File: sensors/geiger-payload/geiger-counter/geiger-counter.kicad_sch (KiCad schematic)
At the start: 38 parts, among them J1 3531, J2 3531, J4 Conn_02x03_Odd_Even, J5 Conn_01x06, J6 Conn_01x03, Q1 MMBTA44, Q2 MMBT3904, Q3 MMBT3904, SW1 SW_Push, SW2 SW_SPDT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

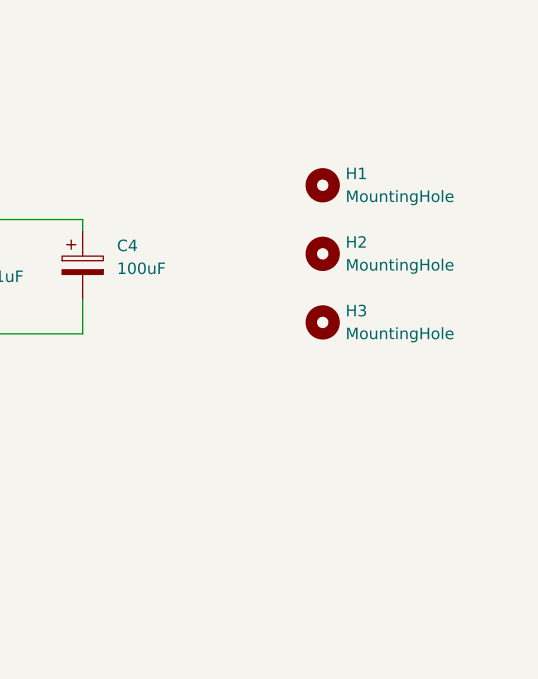
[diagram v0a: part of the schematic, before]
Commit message: Add pcb corrections
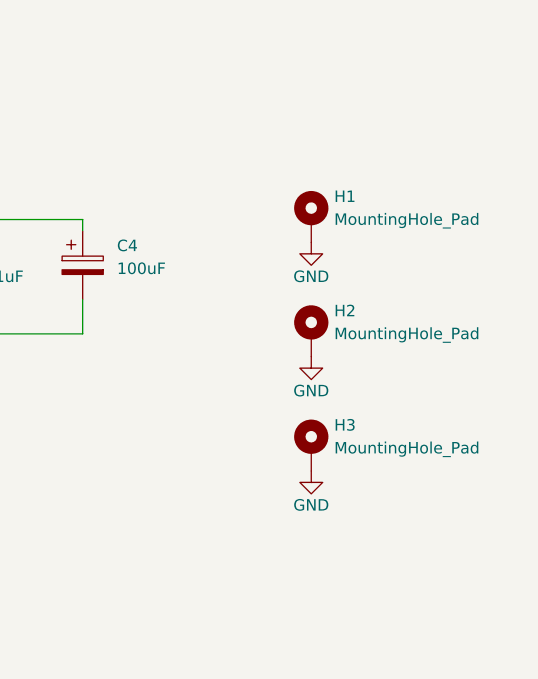
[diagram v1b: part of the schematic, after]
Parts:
- removed H1, H2, H3: MountingHole, MountingHole:MountingHole_2.2mm_M2_DIN965_Pad_TopOnly, symbol Mechanical:MountingHole
- added H1, H2, H3: MountingHole_Pad, MountingHole:MountingHole_2.2mm_M2_Pad, symbol Mechanical:MountingHole_Pad
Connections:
- net GND: now also H1.1, H2.1, H3.1
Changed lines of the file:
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@@
+    )
+  )
+  (symbol (lib_id "Mechanical:MountingHole_Pad") (at 250.19 133.35 0) (unit 1)
+    (in_bom yes) (on_board yes) (dnp no) (fields_autoplaced)
+    (property "Reference" "H3" (at 252.73 130.81 0)
+      (effects (font (size 1.27 1.27)) (justify left))
+    )
+    (property "Value" "MountingHole_Pad" (at 252.73 133.35 0)
+      (effects (font (size 1.27 1.27)) (justify left))
+    )
+    (property "Footprint" "MountingHole:MountingHole_2.2mm_M2_Pad" (at 250.19 133.35 0)
+      (effects (font (size 1.27 1.27)) hide)
+    )
+    (property "Datasheet" "~" (at 250.19 133.35 0)
+      (effects (font (size 1.27 1.27)) hide)
+    )
+    (pin "1")
+    (instances
+      (project "geiger-counter"
+        (path "/7804f9af-0587-435d-9482-64f925891946"
+          (reference "H3") (unit 1)
+        )
+      )
     )
   )
@@
         (path "/7804f9af-0587-435d-9482-64f925891946"
           (reference "#PWR08") (unit 1)
+        )
+      )
+    )
+  )
+  (symbol (lib_id "Mechanical:MountingHole_Pad") (at 250.19 107.95 0) (unit 1)
+    (in_bom yes) (on_board yes) (dnp no) (fields_autoplaced)
+    (property "Reference" "H1" (at 252.73 105.41 0)
+      (effects (font (size 1.27 1.27)) (justify left))
+    )
+    (property "Value" "MountingHole_Pad" (at 252.73 107.95 0)
+      (effects (font (size 1.27 1.27)) (justify left))
+    )
+    (property "Footprint" "MountingHole:MountingHole_2.2mm_M2_Pad" (at 250.19 107.95 0)
+      (effects (font (size 1.27 1.27)) hide)
+    )
+    (property "Datasheet" "~" (at 250.19 107.95 0)
+      (effects (font (size 1.27 1.27)) hide)
+    )
+    (pin "1")
+    (instances
+      (project "geiger-counter"
+        (path "/7804f9af-0587-435d-9482-64f925891946"
+          (reference "H1") (unit 1)
         )
       )
@@
     )
   )
+  (symbol (lib_id "power:GND") (at 250.19 123.19 0) (unit 1)
+    (in_bom yes) (on_board yes) (dnp no)
+    (property "Reference" "#PWR032" (at 250.19 129.54 0)
+      (effects (font (size 1.27 1.27)) hide)
+    )
+    (property "Value" "GND" (at 250.19 127 0)
+      (effects (font (size 1.27 1.27)))
+    )
+    (property "Footprint" "" (at 250.19 123.19 0)
+      (effects (font (size 1.27 1.27)) hide)
+    )
+    (property "Datasheet" "" (at 250.19 123.19 0)
+      (effects (font (size 1.27 1.27)) hide)
+    )
+    (pin "1")
+    (instances
+      (project "geiger-counter"
+        (path "/7804f9af-0587-435d-9482-64f925891946"
+          (reference "#PWR032") (unit 1)
+        )
+      )
+    )
+  )
   (symbol (lib_id "Transistor_BJT:MMBT3904") (at 104.14 55.88 0) (mirror y) (unit 1)
     (in_bom yes) (on_board yes) (dnp no)
@@
     )
   )
-  (symbol (lib_id "Mechanical:MountingHole") (at 251.46 104.14 0) (unit 1)
-    (in_bom yes) (on_board yes) (dnp no) (fields_autoplaced)
-    (property "Reference" "H1" (at 254 102.87 0)
-      (effects (font (size 1.27 1.27)) (justify left))
-    )
-    (property "Value" "MountingHole" (at 254 105.41 0)
-      (effects (font (size 1.27 1.27)) (justify left))
-    )
-    (property "Footprint" "MountingHole:MountingHole_2.2mm_M2_DIN965_Pad_TopOnly" (at 251.46 104.14 0)
-      (effects (font (size 1.27 1.27)) hide)
-    )
-    (property "Datasheet" "~" (at 251.46 104.14 0)
-      (effects (font (size 1.27 1.27)) hide)
-    )
-    (instances
-      (project "geiger-counter"
-        (path "/7804f9af-0587-435d-9482-64f925891946"
-          (reference "H1") (unit 1)
-        )
-      )
-    )
-  )
   (symbol (lib_id "Device:C") (at 80.01 78.74 0) (unit 1)
     (in_bom yes) (on_board yes) (dnp no) (fields_autoplaced)
@@
     )
   )
-  (symbol (lib_id "Mechanical:MountingHole") (at 251.46 111.76 0) (unit 1)
-    (in_bom yes) (on_board yes) (dnp no) (fields_autoplaced)
-    (property "Reference" "H2" (at 254 110.49 0)
-      (effects (font (size 1.27 1.27)) (justify left))
-    )
-    (property "Value" "MountingHole" (at 254 113.03 0)
-      (effects (font (size 1.27 1.27)) (justify left))
-    )
-    (property "Footprint" "MountingHole:MountingHole_2.2mm_M2_DIN965_Pad_TopOnly" (at 251.46 111.76 0)
-      (effects (font (size 1.27 1.27)) hide)
-    )
-    (property "Datasheet" "~" (at 251.46 111.76 0)
-      (effects (font (size 1.27 1.27)) hide)
-    )
-    (instances
-      (project "geiger-counter"
-        (path "/7804f9af-0587-435d-9482-64f925891946"
-          (reference "H2") (unit 1)
-        )
-      )
-    )
-  )
   (symbol (lib_id "Geiger:MMBTA44") (at 111.76 44.45 0) (unit 1)
     (in_bom yes) (on_board yes) (dnp no) (fields_autoplaced)
@@
     )
   )
-  (symbol (lib_id "Mechanical:MountingHole") (at 251.46 119.38 0) (unit 1)
-    (in_bom yes) (on_board yes) (dnp no) (fields_autoplaced)
-    (property "Reference" "H3" (at 254 118.11 0)
-      (effects (font (size 1.27 1.27)) (justify left))
-    )
-    (property "Value" "MountingHole" (at 254 120.65 0)
-      (effects (font (size 1.27 1.27)) (justify left))
-    )
-    (property "Footprint" "MountingHole:MountingHole_2.2mm_M2_DIN965_Pad_TopOnly" (at 251.46 119.38 0)
-      (effects (font (size 1.27 1.27)) hide)
-    )
-    (property "Datasheet" "~" (at 251.46 119.38 0)
-      (effects (font (size 1.27 1.27)) hide)
-    )
-    (instances
-      (project "geiger-counter"
-        (path "/7804f9af-0587-435d-9482-64f925891946"
-          (reference "H3") (unit 1)
-        )
-      )
-    )
-  )
   (symbol (lib_id "power:GND") (at 201.93 57.15 0) (unit 1)
     (in_bom yes) (on_board yes) (dnp no) (fields_autoplaced)
@@
         (path "/7804f9af-0587-435d-9482-64f925891946"
           (reference "#PWR03") (unit 1)
+        )
+      )
+    )
+  )
+  (symbol (lib_id "power:GND") (at 250.19 110.49 0) (unit 1)
+    (in_bom yes) (on_board yes) (dnp no)
+    (property "Reference" "#PWR033" (at 250.19 116.84 0)
+      (effects (font (size 1.27 1.27)) hide)
+    )
+    (property "Value" "GND" (at 250.19 114.3 0)
+      (effects (font (size 1.27 1.27)))
+    )
+    (property "Footprint" "" (at 250.19 110.49 0)
+      (effects (font (size 1.27 1.27)) hide)
+    )
+    (property "Datasheet" "" (at 250.19 110.49 0)
+      (effects (font (size 1.27 1.27)) hide)
+    )
+    (pin "1")
+    (instances
+      (project "geiger-counter"
+        (path "/7804f9af-0587-435d-9482-64f925891946"
+          (reference "#PWR033") (unit 1)
         )
       )
@@
         )
       )
+    )
+  )
+  (symbol (lib_id "Mechanical:MountingHole_Pad") (at 250.19 120.65 0) (unit 1)
+    (in_bom yes) (on_board yes) (dnp no) (fields_autoplaced)
+    (property "Reference" "H2" (at 252.73 118.11 0)
+      (effects (font (size 1.27 1.27)) (justify left))
+    )
+    (property "Value" "MountingHole_Pad" (at 252.73 120.65 0)
+      (effects (font (size 1.27 1.27)) (justify left))
+    )
+    (property "Footprint" "MountingHole:MountingHole_2.2mm_M2_Pad" (at 250.19 120.65 0)
+      (effects (font (size 1.27 1.27)) hide)
+    )
+    (property "Datasheet" "~" (at 250.19 120.65 0)
+      (effects (font (size 1.27 1.27)) hide)
+    )
+    (pin "1")
+    (instances
+      (project "geiger-counter"
+        (path "/7804f9af-0587-435d-9482-64f925891946"
+          (reference "H2") (unit 1)
+        )
+      )
+    )
+  )
+  (symbol (lib_id "power:GND") (at 250.19 135.89 0) (unit 1)
+    (in_bom yes) (on_board yes) (dnp no)
+    (property "Reference" "#PWR031" (at 250.19 142.24 0)
+      (effects (font (size 1.27 1.27)) hide)
+    )
+    (property "Value" "GND" (at 250.19 139.7 0)
+      (effects (font (size 1.27 1.27)))
+    )
+    (property "Footprint" "" (at 250.19 135.89 0)
+      (effects (font (size 1.27 1.27)) hide)
+    )
+    (property "Datasheet" "" (at 250.19 135.89 0)
+      (effects (font (size 1.27 1.27)) hide)
+    )
+    (pin "1")
+    (instances
+      (project "geiger-counter"
+        (path "/7804f9af-0587-435d-9482-64f925891946"
+          (reference "#PWR031") (unit 1)
+        )
+      )

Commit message: pcb alterations due to part sourcing
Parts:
- removed BT1: 3V, Battery:BatteryHolder_Keystone_2468_2xAAA, symbol Device:Battery
- removed J1, J2: 3531, Geiger Footprints:FUSE_3531, symbol Geiger:3531
- added BT1: ~, Geiger Footprints:1022, symbol Geiger:2AAA
- added J1, J2: ~, Geiger Footprints:FUSE_3514, symbol Geiger:3514
- J4: footprint Connector_PinHeader_1.27mm:PinHeader_2x03_P1.27mm_Vertical -> Connector_PinHeader_2.54mm:PinHeader_2x03_P2.54mm_Vertical
- J5: footprint Connector_PinHeader_1.27mm:PinHeader_1x06_P1.27mm_Vertical -> Connector_PinHeader_2.54mm:PinHeader_1x06_P2.54mm_Vertical
- J6: footprint Connector_PinHeader_1.27mm:PinHeader_1x03_P1.27mm_Vertical -> Connector_PinHeader_2.54mm:PinHeader_1x03_P2.54mm_Vertical
- L1: footprint Inductor_SMD:L_10.4x10.4_H4.8 -> Inductor_SMD:L_Bourns-SRN8040_8x8.15mm
- RV1: footprint Potentiometer_SMD:Potentiometer_ACP_CA9-VSMD_Vertical -> Geiger Footprints:G43A
- SW2: footprint Button_Switch_SMD:SW_SPDT_CK-JS102011SAQN -> Geiger Footprints:TP-33103
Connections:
- net GND: now also BT1.1 (-)
- net at R4.1: now also J1.1, J1.2
- net at SW2.2 (B): now also BT1.2 (+)
- net at C1.1, R1.1: now also J2.1, J2.2
- new net: BT1.3, BT1.4

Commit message: pcb design changes
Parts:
- C1, C2, C5: footprint Capacitor_SMD:C_1206_3216Metric -> Capacitor_SMD:C_0805_2012Metric
- L1: footprint Inductor_SMD:L_Bourns-SRN8040_8x8.15mm -> Inductor_SMD:L_Changjiang_FNR6045S
- R1, R10, R2, R3, R5, R6, R7, R8, R9: footprint Resistor_SMD:R_1206_3216Metric -> Resistor_SMD:R_0805_2012Metric
- SW1: footprint Button_Switch_SMD:SW_Push_1P1T_NO_6x6mm_H9.5mm -> Button_Switch_SMD:SW_Push_1P1T_XKB_TS-1187A
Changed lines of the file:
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@@
       (effects (font (size 1.27 1.27)))
     )
-    (property "Footprint" "Resistor_SMD:R_1206_3216Metric" (at 123.19 145.288 90)
+    (property "Footprint" "Resistor_SMD:R_0805_2012Metric" (at 123.19 145.288 90)
       (effects (font (size 1.27 1.27)) hide)
     )
@@
       (effects (font (size 1.27 1.27)) (justify left))
     )
-    (property "Footprint" "Capacitor_SMD:C_1206_3216Metric" (at 210.5152 116.84 0)
+    (property "Footprint" "Capacitor_SMD:C_0805_2012Metric" (at 210.5152 116.84 0)
       (effects (font (size 1.27 1.27)) hide)
     )
@@
       (effects (font (size 1.27 1.27)) (justify left))
     )
-    (property "Footprint" "Resistor_SMD:R_1206_3216Metric" (at 99.822 31.75 90)
+    (property "Footprint" "Resistor_SMD:R_0805_2012Metric" (at 99.822 31.75 90)
       (effects (font (size 1.27 1.27)) hide)
     )
@@
       (effects (font (size 1.27 1.27)) (justify left))
     )
-    (property "Footprint" "Resistor_SMD:R_1206_3216Metric" (at 229.362 29.21 90)
+    (property "Footprint" "Resistor_SMD:R_0805_2012Metric" (at 229.362 29.21 90)
       (effects (font (size 1.27 1.27)) hide)
     )
@@
       (effects (font (size 1.27 1.27)))
     )
-    (property "Footprint" "Resistor_SMD:R_1206_3216Metric" (at 87.63 46.228 90)
+    (property "Footprint" "Resistor_SMD:R_0805_2012Metric" (at 87.63 46.228 90)
       (effects (font (size 1.27 1.27)) hide)
     )
@@
       (effects (font (size 1.27 1.27)) (justify left))
     )
-    (property "Footprint" "Resistor_SMD:R_1206_3216Metric" (at 28.702 78.74 90)
+    (property "Footprint" "Resistor_SMD:R_0805_2012Metric" (at 28.702 78.74 90)
       (effects (font (size 1.27 1.27)) hide)
     )
@@
       (effects (font (size 1.27 1.27)) (justify left))
     )
-    (property "Footprint" "Resistor_SMD:R_1206_3216Metric" (at 212.852 41.91 90)
+    (property "Footprint" "Resistor_SMD:R_0805_2012Metric" (at 212.852 41.91 90)
       (effects (font (size 1.27 1.27)) hide)
     )
@@
       (effects (font (size 1.27 1.27)) (justify left))
     )
-    (property "Footprint" "Capacitor_SMD:C_1206_3216Metric" (at 80.9752 82.55 0)
+    (property "Footprint" "Capacitor_SMD:C_0805_2012Metric" (at 80.9752 82.55 0)
       (effects (font (size 1.27 1.27)) hide)
     )
@@
       (effects (font (size 1.27 1.27)) (justify right))
     )
-    (property "Footprint" "Resistor_SMD:R_1206_3216Metric" (at 216.408 55.88 90)
+    (property "Footprint" "Resistor_SMD:R_0805_2012Metric" (at 216.408 55.88 90)
       (effects (font (size 1.27 1.27)) hide)
     )
@@
       (effects (font (size 1.27 1.27)) (justify left))
     )
-    (property "Footprint" "Resistor_SMD:R_1206_3216Metric" (at 41.402 125.73 90)
+    (property "Footprint" "Resistor_SMD:R_0805_2012Metric" (at 41.402 125.73 90)
       (effects (font (size 1.27 1.27)) hide)
     )
@@
       (effects (font (size 1.27 1.27)) (justify left))
     )
-    (property "Footprint" "Button_Switch_SMD:SW_Push_1P1T_NO_6x6mm_H9.5mm" (at 114.3 166.37 0)
+    (property "Footprint" "Button_Switch_SMD:SW_Push_1P1T_XKB_TS-1187A" (at 114.3 166.37 0)
       (effects (font (size 1.27 1.27)) hide)
     )
@@
       (effects (font (size 1.27 1.27)) (justify left))
     )
-    (property "Footprint" "Resistor_SMD:R_1206_3216Metric" (at 78.232 58.42 90)
+    (property "Footprint" "Resistor_SMD:R_0805_2012Metric" (at 78.232 58.42 90)
       (effects (font (size 1.27 1.27)) hide)
     )
@@
       (effects (font (size 1.27 1.27)) (justify left))
     )
-    (property "Footprint" "Capacitor_SMD:C_1206_3216Metric" (at 202.8952 53.34 0)
+    (property "Footprint" "Capacitor_SMD:C_0805_2012Metric" (at 202.8952 53.34 0)
       (effects (font (size 1.27 1.27)) hide)
     )
@@
       (effects (font (size 1.27 1.27)) (justify left))
     )
-    (property "Footprint" "Inductor_SMD:L_Bourns-SRN8040_8x8.15mm" (at 113.03 31.75 0)
-      (effects (font (size 1.27 1.27)) hide)
-    )
+    (property "Footprint" "Inductor_SMD:L_Changjiang_FNR6045S" (at 113.03 31.75 0)
+      (effects (font (size 1.27 1.27)) hide)
+    )
